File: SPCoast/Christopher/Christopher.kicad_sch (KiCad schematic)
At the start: 45 parts, among them SW813 813, SW815 815, SW817 817, SW900 815A

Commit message: fix(kicad): approach circuits end in T; desk tokens follow
Plants: Christopher 1NA/2NA/1SA/2SA, GilroyCalTrain 1NA/1SA, GilroyInterchange
1SA, Sargent 1NA/1SA/2SA gain the final T (ADR 0003 D4). Sargent's reference
Corporal:2NA becomes Corporal:2NAT, the circuit Corporal draws.

Desk (South-cTc sheets): IndicationToken follows the plants for Christopher,
GilroyCalTrain, GilroyInterchange; Corporal 1SA becomes 1SAT (the plant already
had it); Christopher 815T2 becomes 815AT1 (the OS circuit of switch 815A).

Not changed, awaiting decisions in the dry-run report: 0<n>T renames (IND,
TK<n>, Interchange, 2NAAT, 2SAT), section 2 of an approach, unnamed circuits,
Watsonville, CP_Watsonville: references, 1TK.

Verified: netlists rebuilt for all affected projects; of 33 desk circuit tokens,
5 now match no plant circuit (was 11): 1TK, CP_Watsonville:SA1,
CP_Watsonville:837T1, Watsonville 1NAK and 2NAK. KiCad closed, no ~*.lck.

Co-Authored-By: Claude Sonnet 5.5 <noreply@anthropic.com>
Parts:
- TC1: value 1NA -> 1NAT
- TC2: value 2NA -> 2NAT
- TC3: value 1SA -> 1SAT
- TC4: value 2SA -> 2SAT
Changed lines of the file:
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@@
 			)
 		)
-		(property "Value" "1SA"
+		(property "Value" "1SAT"
 			(at 53.85 97.54 0)
 			(show_name no)
@@
 			)
 		)
-		(property "Value" "2NA"
+		(property "Value" "2NAT"
 			(at 208.79 64.52 0)
 			(show_name no)
@@
 			)
 		)
-		(property "Value" "1NA"
+		(property "Value" "1NAT"
 			(at 208.79 97.54 0)
 			(show_name no)
@@
 			)
 		)
-		(property "Value" "2SA"
+		(property "Value" "2SAT"
 			(at 53.85 64.52 0)
 			(show_name no)

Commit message: fix(kicad): remaining class I circuits take the 0<n>T form
Owner-approved numbers: Luchessa 2SAT -> 02T; Christopher IND -> 01T;
Corporal IND -> 01T; GilroyInterchange Interchange -> 01T and TK1 -> 02T
(passing-track main and siding merged into class I). Desk lamp 1TK on
GilroyInterchange column 4 becomes 02T.

Verified: netlists rebuilt for the five projects; every 0<n>T is unique within
its plant; desk circuit tokens that match no plant circuit are down to four
(CP_Watsonville:SA1, CP_Watsonville:837T1, Watsonville 1NAK and 2NAK).

Co-Authored-By: Claude Sonnet 5.5 <noreply@anthropic.com>
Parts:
- TC5: value IND -> 01T
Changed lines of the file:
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@@
 			)
 		)
-		(property "Value" "IND"
+		(property "Value" "01T"
 			(at 130.05 114.05 0)
 			(show_name no)

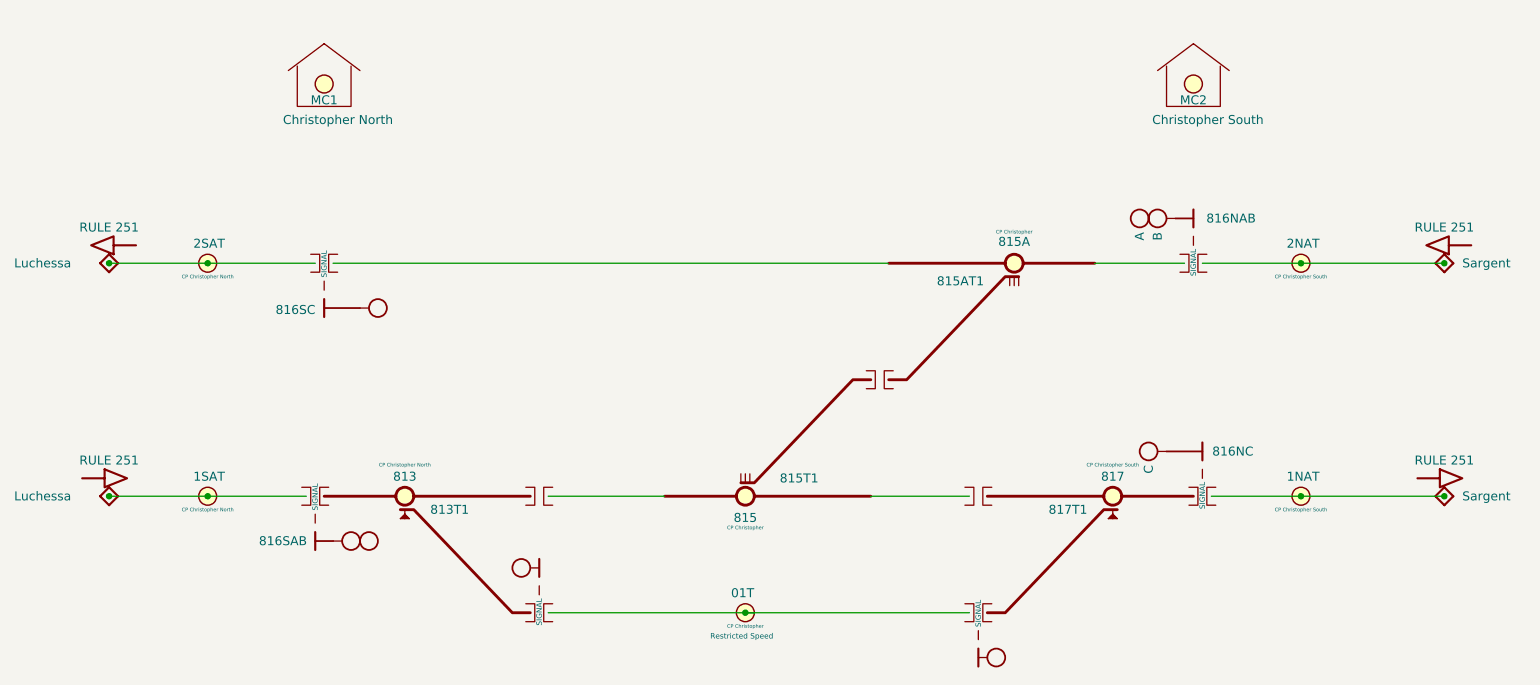
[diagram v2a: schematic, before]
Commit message: SPCoast: owner's edits: schematics synced with the revised symbol libraries (baseline)
Update Symbols from Library on all plant and desk sheets; CP values for
Christopher, GilroyInterchange and Luchessa; Restricted Speed markers
consolidated in Corporal, Luchessa and Sargent.

Observed in the diff, not changed by the sweep that follows: CP changed on 23
symbols (Christopher: prefix removed, 815/815A/IND now Christopher North) and
added on 12 (GilroyInterchange); two lamps' Color reset to their symbol variant
(Christopher LMP93 red -> yellow, Sargent LMP133 yellow -> red).

Verified: netlists keep their net counts (Christopher 33, Corporal 26,
GilroyCalTrain 27, GilroyInterchange 22, Luchessa 34, Sargent 18, Watsonville
96, South-cTc 341); desk compiles to 75 appliances, 137 bindings, 14 columns;
no root-UUID regression.

Co-Authored-By: Claude Sonnet 5.5 <noreply@anthropic.com>
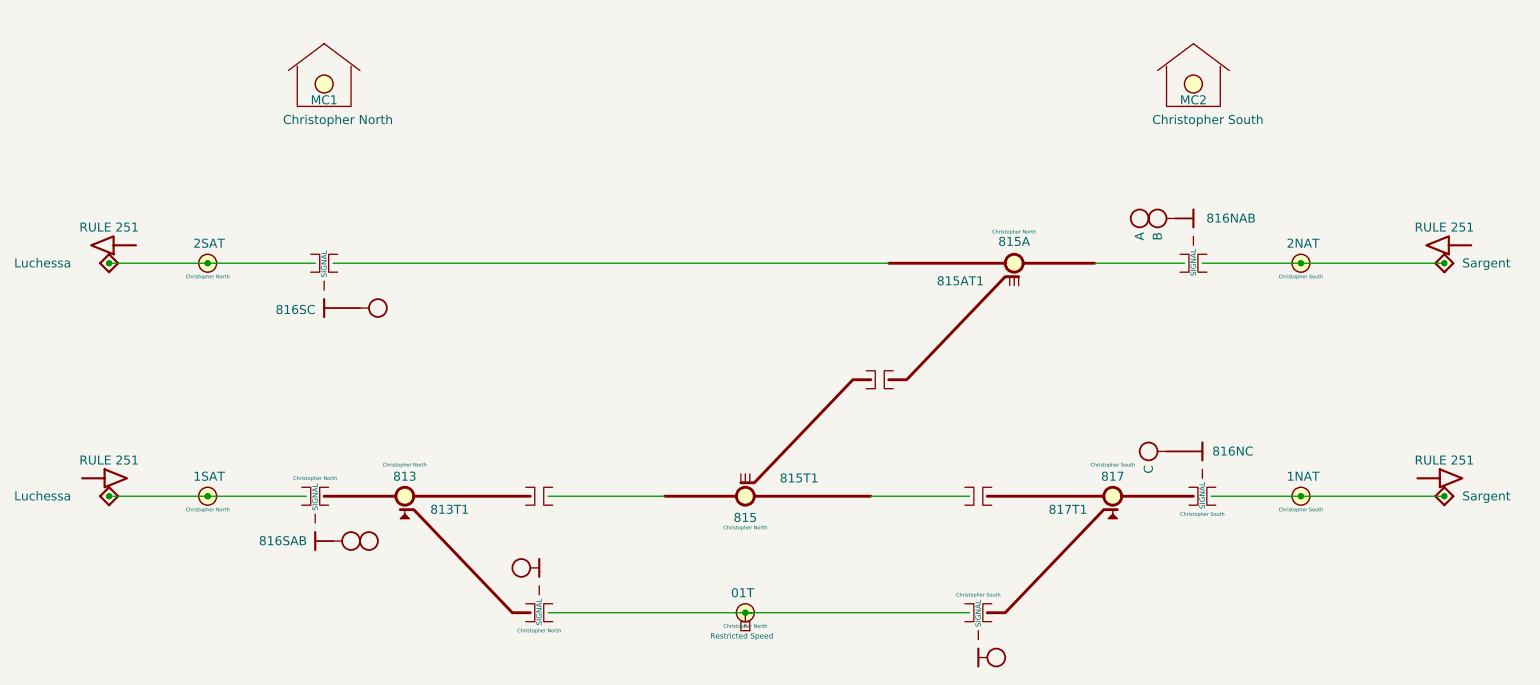
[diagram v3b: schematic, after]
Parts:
- B6, B8: CP (none) -> Christopher North
- B7, B9: CP (none) -> Christopher South
- MC1, S4, S5, SW813, TC3, TC4: CP CP Christopher North -> Christopher North
- MC2, S3, S6: CP CP Christopher South -> Christopher North
- SW815, SW900, TC5: CP CP Christopher -> Christopher North
- SW817, TC1, TC2: CP CP Christopher South -> Christopher South
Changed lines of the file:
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@@
 			)
 		)
-		(property "Description" "Maintainer Bungalow"
-			(at 195.58 47.63 0)
+		(property "Description" "Rrepresents the Control Point Maintainer Bungalow (plus optional Maintainer Call)"
+			(at 195.58 47.625 0)
 			(hide yes)
 			(show_name no)
@@
 			)
 		)
-		(property "CP" "CP Christopher North"
+		(property "CP" "Christopher North"
 			(at 55.88 102.23 0)
 			(show_name no)
@@
 			)
 		)
-		(property "CP" "CP Christopher North"
+		(property "CP" "Christopher North"
 			(at 72.39 71.12 0)
 			(hide yes)
@@
 			)
 		)
-		(property "CP" "CP Christopher"
+		(property "CP" "Christopher North"
 			(at 132.08 104.78 0)
 			(show_name no)
@@
 			)
 		)
-		(property "CP" "CP Christopher North"
+		(property "CP" "Christopher North"
 			(at 83.82 95.88 0)
 			(show_name no)
@@
 			)
 		)
-		(property "Description" "Insulated Rail Joint"
+		(property "Description" "Insulated Rail Joint with Signal"
 			(at 195.58 67.31 0)
 			(hide yes)
@@
 			)
 		)
-		(property "CP" "CP Christopher North"
+		(property "CP" "Christopher North"
 			(at 71.12 104.14 0)
 			(hide yes)
@@
 			)
 		)
-		(property "Description" "Restricted speed: Standard Code Rule 105, GCOR 6.28: This is the foundational rule governing most industrial tracks. It mandates that trains or engines must move at a speed that allows them to stop within half the range of vision short of a train, engine, car, stop signal, derail, or switch improperly lined. It also requires crew members to look out for track obstructions"
+		(property "Description" "Restricted speed: Standard Code Rule 105, GCOR 6.28: Movement on Other Than Main Track. This is the foundational rule governing most industrial tracks. It mandates that trains or engines must move at a speed that allows them to stop within half the range of vision short of a train, engine, car, stop signal, derail, or switch improperly lined. It also requires crew members to look out for track obstructions"
 			(at 135.255 114.935 0)
 			(hide yes)
@@
 			)
 		)
-		(property "CP" "CP Christopher North"
+		(property "CP" "Christopher North"
 			(at 72.39 41.91 0)
 			(hide yes)
@@
 			)
 		)
-		(property "CP" "CP Christopher"
+		(property "CP" "Christopher North"
 			(at 132.08 118.74 0)
 			(show_name no)
@@
 			)
 		)
-		(property "Description" "Maintainer Bungalow"
-			(at 72.39 47.63 0)
+		(property "Description" "Rrepresents the Control Point Maintainer Bungalow (plus optional Maintainer Call)"
+			(at 72.39 47.625 0)
 			(hide yes)
 			(show_name no)
@@
 			)
 		)
-		(property "Description" "Governs movements on tracks where signals are only configured for  one direction.  Under this rule, signal indications supersede the superiority of trains for movements operating with the current of traffic.  Moving against this traffic direction requires explicit authority (such as a train order or track warrant)."
+		(property "Description" "Rule 251 (Track Signaled in One Direction): Governs movements on tracks where signals are only configured for  one direction.  Under this rule, signal indications supersede the superiority of trains for movements operating with the current of traffic.  Moving against this traffic direction requires explicit authority (such as a train order or track warrant)."
 			(at 227.965 71.755 0)
 			(hide yes)
@@
 			)
 		)
-		(property "Description" "Insulated Rail Joint"
+		(property "Description" "Insulated Rail Joint with Signal"
 			(at 72.39 67.31 0)
 			(hide yes)
@@
 			)
 		)
-		(property "CP" "CP Christopher"
+		(property "CP" "Christopher North"
 			(at 170.18 62.86 0)
 			(show_name no)
@@
 			)
 		)
-		(property "CP" "CP Christopher South"
+		(property "CP" "Christopher North"
 			(at 195.58 41.91 0)
 			(hide yes)
@@
 			)
 		)
-		(property "CP" "CP Christopher South"
+		(property "CP" "Christopher South"
 			(at 210.82 69.21 0)
 			(show_name no)
@@
 			)
 		)
-		(property "CP" ""
-			(at 73.025 102.235 0)
+		(property "CP" "Christopher North"
+			(at 71.12 97.79 0)
 			(show_name no)
 			(do_not_autoplace no)
@@
 					(color 72 72 72 1)
 				)
-				(justify right)
 			)
 		)
@@
 			)
 		)
-		(property "CP" "CP Christopher South"
+		(property "CP" "Christopher North"
 			(at 196.85 96.52 0)
 			(hide yes)
@@
 			)
 		)
-		(property "CP" "CP Christopher South"
+		(property "CP" "Christopher South"
 			(at 210.82 102.23 0)
 			(show_name no)
@@
 			)
 		)
-		(property "CP" ""
-			(at 194.945 98.425 0)
+		(property "CP" "Christopher South"
+			(at 196.85 102.87 0)
 			(show_name no)
 			(do_not_autoplace no)
@@
 					(color 72 72 72 1)
 				)
-				(justify right)
 			)
 		)
@@
 			)
 		)
-		(property "CP" "CP Christopher South"
+		(property "CP" "Christopher South"
 			(at 184.15 95.88 0)
 			(show_name no)
@@
 			)
 		)
-		(property "CP" "CP Christopher South"
+		(property "CP" "Christopher North"
 			(at 195.58 63.5 0)
 			(hide yes)
@@
 			)
 		)
-		(property "CP" "CP Christopher North"
+		(property "CP" "Christopher North"
 			(at 55.88 69.21 0)
 			(show_name no)
@@
 			)
 		)
-		(property "CP" ""
-			(at 100.965 114.935 0)
+		(property "CP" "Christopher North"
+			(at 102.87 119.38 0)
 			(show_name no)
 			(do_not_autoplace no)
@@
 					(color 72 72 72 1)
 				)
-				(justify right)
 			)
 		)
@@
 			)
 		)
-		(property "CP" ""
-			(at 167.005 118.745 0)
+		(property "CP" "Christopher South"
+			(at 165.1 114.3 0)
 			(show_name no)
 			(do_not_autoplace no)
@@
 					(color 72 72 72 1)
 				)
-				(justify right)
 			)
 		)
@@
 			)
 		)
-		(property "Description" "Governs movements on tracks where signals are only configured for  one direction.  Under this rule, signal indications supersede the superiority of trains for movements operating with the current of traffic.  Moving against this traffic direction requires explicit authority (such as a train order or track warrant)."
+		(property "Description" "Rule 251 (Track Signaled in One Direction): Governs movements on tracks where signals are only configured for  one direction.  Under this rule, signal indications supersede the superiority of trains for movements operating with the current of traffic.  Moving against this traffic direction requires explicit authority (such as a train order or track warrant)."
 			(at 38.735 71.755 0)
 			(hide yes)

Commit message: chore(kicad): sweep instance Role/Kind and stale fields to the library vocabulary
Scripted, one pass over every sheet except Watsonville (open in KiCad, locked):
- Role/Kind of placed symbols refreshed from the library by lib_id: 10 Role
  (MAIN HOUSE CONTROLLED_POINT -> CONTROL_POINT, Rule251-DoT empty) and 17 Kind
  (IRJ-Signal IRJ -> IRJ_SIGNAL x7, Mast_Single/Double swaps, HandThrow
  -> SWITCH_MANUAL, Derail, PanelLock -> LOCK_LEVER, NextCP).
- Stale instance fields dropped where the library no longer has them: 39 Name,
  28 Direction (all empty or retired), 5 CP on Bumper and IRJ symbols.
- Orphan embedded copies of the retired symbol Rule6.28-OtherThanMain removed
  from two sheets (unused).

Not done: Watsonville (locked); CMRInet -> CMRI (library Kind still CMRInet);
fields new to the library (MAIN HOUSE Kind, switch Indications) are not copied
onto instances, the compiler will read library defaults by lib_id; Rulebook
fields stay until the compiler stops requiring them.

Verified: per-symbol before/after comparison shows only these changes, same
symbol sets, positions and lib_ids; netlists keep their net counts (Christopher
33, Corporal 26, GilroyCalTrain 27, GilroyInterchange 22, Luchessa 34, Sargent
18, South-cTc 341); desk still 75 appliances, 137 bindings, 14 columns.

Co-Authored-By: Claude Sonnet 5.5 <noreply@anthropic.com>
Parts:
- B4, B5: Kind IRJ -> IRJ_SIGNAL
- DOT2, DOT3: Name Track Signaled in One Direction -> (none)
- DOT5: Name Movement on Other Than Main Track -> (none)
- HOUSE1, HOUSE3: Role CONTROLLED_POINT -> CONTROL_POINT
- S3, S5: Kind MAST_DOUBLE -> MAST_SINGLE
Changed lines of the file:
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@@
 			)
 		)
-		(property "Role" "CONTROLLED_POINT"
+		(property "Role" "CONTROL_POINT"
 			(at 195.58 41.91 0)
 			(hide yes)
@@
 			)
 		)
-		(property "Kind" "MAST_DOUBLE"
+		(property "Kind" "MAST_SINGLE"
 			(at 72.39 71.12 0)
 			(hide yes)
@@
 			)
 		)
-		(property "Kind" "IRJ"
+		(property "Kind" "IRJ_SIGNAL"
 			(at 195.58 67.31 0)
 			(hide yes)
@@
 			)
 		)
-		(property "Name" "Movement on Other Than Main Track"
-			(at 130.81 123.825 0)
-			(hide yes)
-			(show_name no)
-			(do_not_autoplace no)
-			(effects
-				(font
-					(size 1.27 1.27)
-				)
-			)
-		)
 		(property "Role" "POLICY"
 			(at 132.08 119.38 0)
@@
 			)
 		)
-		(property "Role" "CONTROLLED_POINT"
+		(property "Role" "CONTROL_POINT"
 			(at 72.39 41.91 0)
 			(hide yes)
@@
 			)
 		)
-		(property "Name" "Track Signaled in One Direction"
-			(at 231.775 60.325 0)
-			(hide yes)
-			(show_name no)
-			(do_not_autoplace no)
-			(effects
-				(font
-					(size 1.27 1.27)
-				)
-			)
-		)
 		(property "Role" "POLICY"
 			(at 231.14 64.77 0)
@@
 			)
 		)
-		(property "Kind" "IRJ"
+		(property "Kind" "IRJ_SIGNAL"
 			(at 72.39 67.31 0)
 			(hide yes)
@@
 			)
 		)
-		(property "Kind" "MAST_DOUBLE"
+		(property "Kind" "MAST_SINGLE"
 			(at 196.85 96.52 0)
 			(hide yes)
@@
 			(hide yes)
 			(show_name no)
-			(do_not_autoplace no)
-			(effects
-				(font
-					(size 1.27 1.27)
-				)
-			)
-		)
-		(property "Name" "Track Signaled in One Direction"
-			(at 42.545 60.325 0)
-			(hide yes)
-			(show_name no)

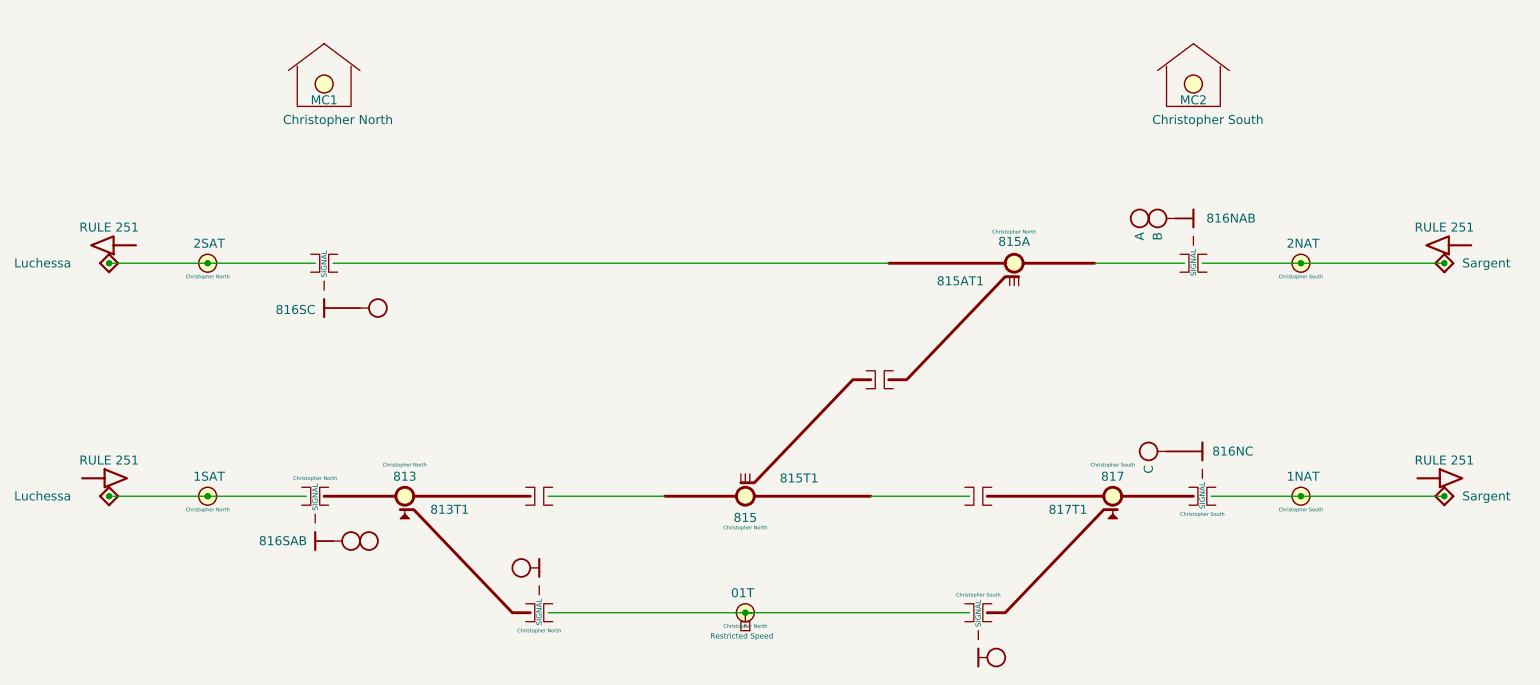
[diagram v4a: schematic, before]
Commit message: SPCoast: owner's edits: Christopher IRJ-Signal CPs set, MC2 CP South (baseline)
Includes an empty Name field that KiCad re-added to every Christopher symbol on save; the next sweep drops it again.

Co-Authored-By: Claude Sonnet 5.5 <noreply@anthropic.com>
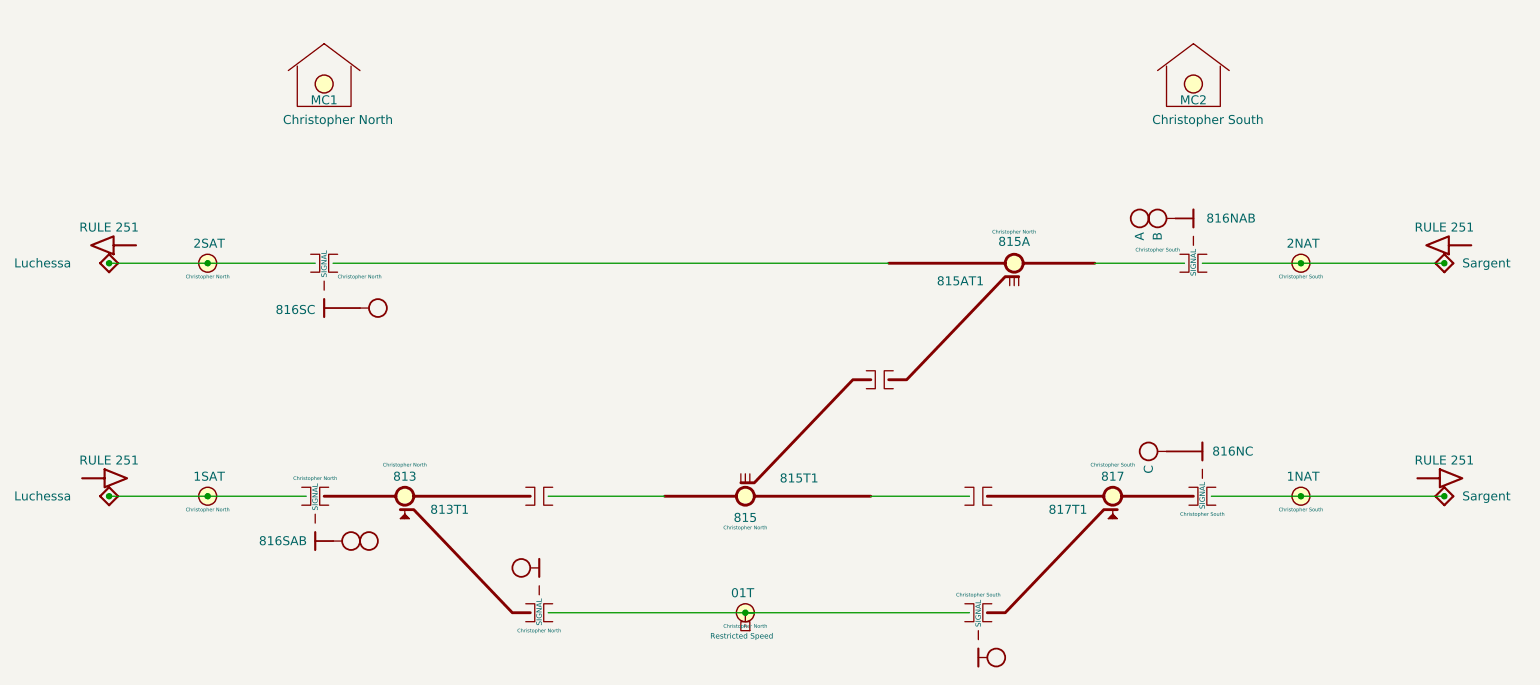
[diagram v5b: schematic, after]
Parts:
- B4: CP (none) -> Christopher South
- B5: CP (none) -> Christopher North
- MC2: CP Christopher North -> Christopher South
